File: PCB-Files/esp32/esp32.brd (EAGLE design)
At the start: 36 x 36 mm, 20 parts, among them SW1 SPST_TACT-KMR2, SW2 SPST_TACT-KMR2, X2 ESP32_WROOM32_SKINNY

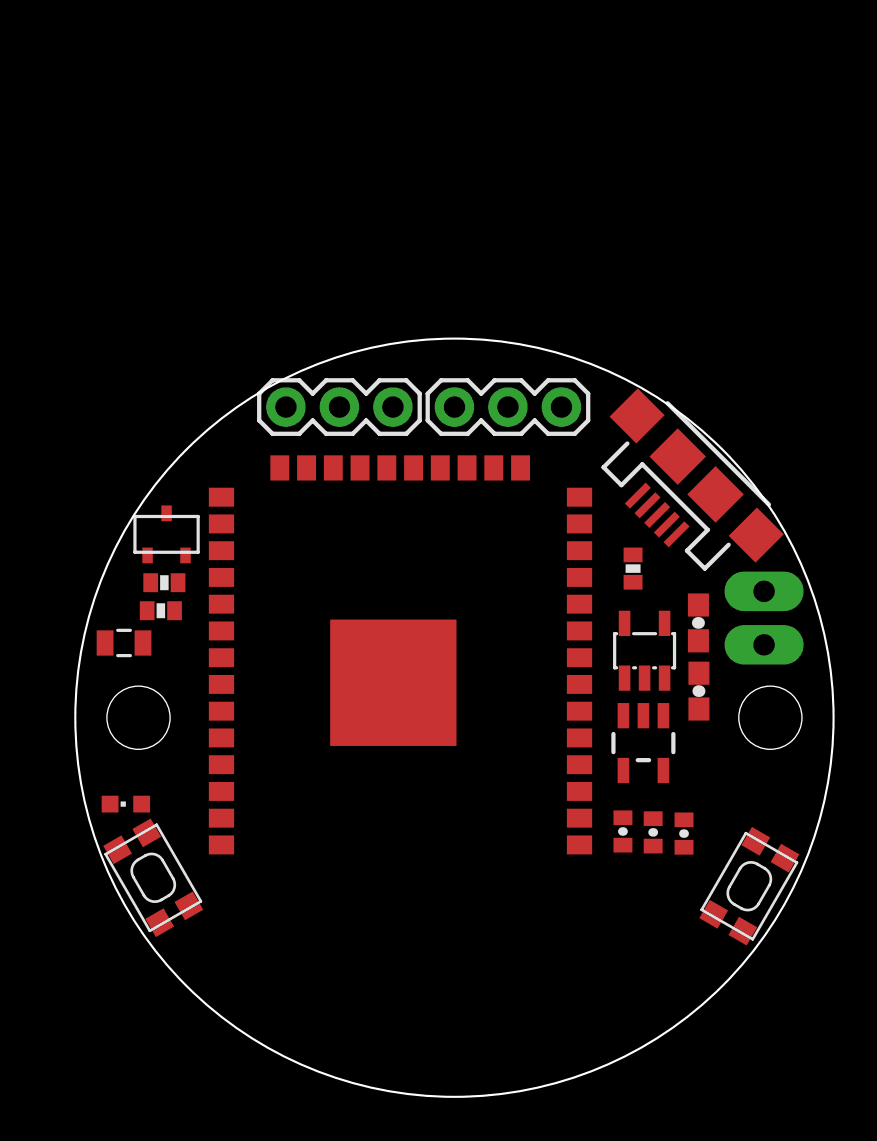
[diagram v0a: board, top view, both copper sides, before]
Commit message: rounded 4-side for class
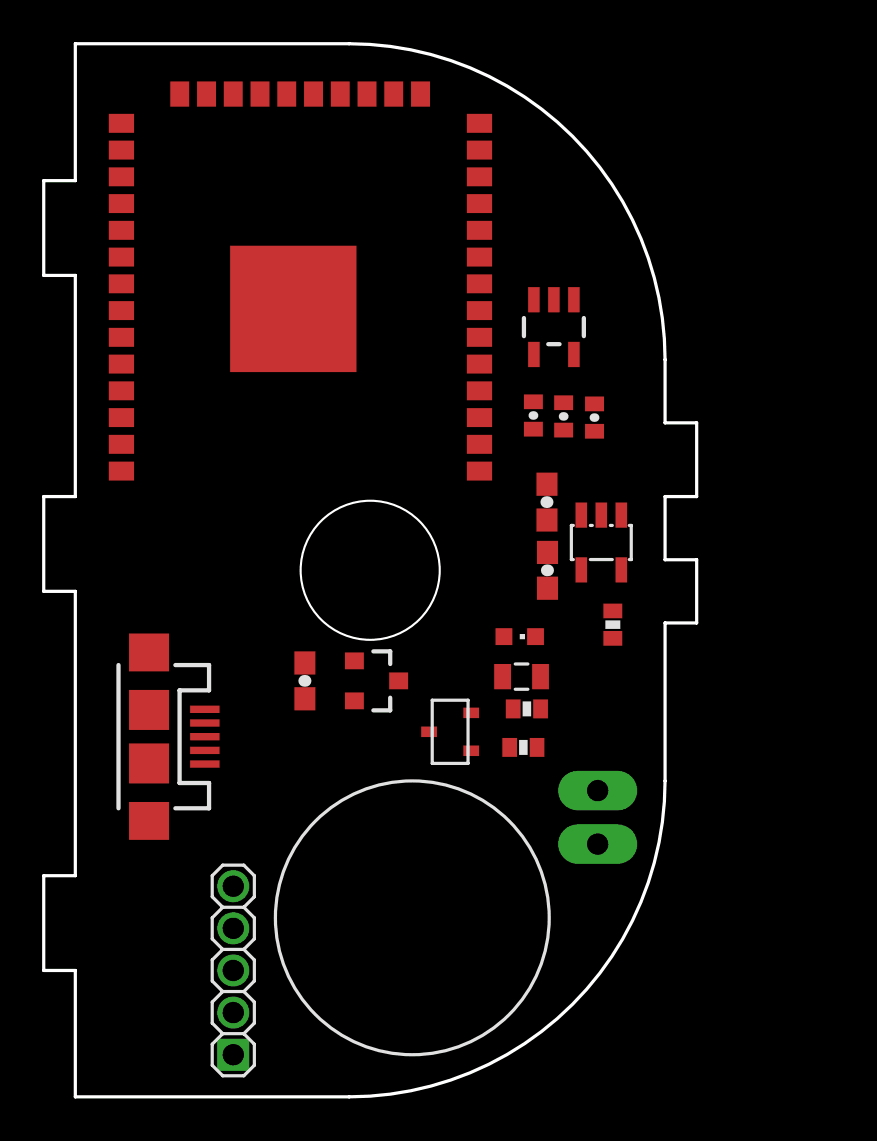
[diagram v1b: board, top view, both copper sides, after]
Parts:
- removed JP2: (no value), SparkFun:1X02_LONGPADS
- removed JP8, JP9: (no value), SparkFun:1X03
- removed SW1, SW2: SPST_TACT-KMR2, adafruit:KMR2
- added C3: 0.1uF, SparkFun:0603-CAP
- added CHARGER: MCP73831/OT, adafruit:SOT23-5L
- added HALL: HALLEFFECT-A1326, Andy_Sigler:SOT23-3
- added JP3: (no value), pinhead:1_05X2MM
- LIPO: value MCP73831/OT -> (none); device adafruit:SOT23-5L -> SparkFun:1X02_LONGPADS
- moved JP1 28.8 mm to (3.50, 17.1), turned to 270 degrees
- moved LED1 20.3 mm to (21.1, 21.9), turned to 270 degrees
- moved C2 20.2 mm to (21.8, 32.4)
- moved C4 20.2 mm to (24.6, 32.2)
- moved REG 20.2 mm to (22.7, 36.5)
- moved C10 20.2 mm to (23.2, 32.3)
- moved R6 18.9 mm to (21.2, 20.0), turned to 180 degrees
- moved R15 18.8 mm to (21.3, 16.6), turned to 0 degrees
- moved X2 18.4 mm to (10.7, 34.7)
- moved R10 18.0 mm to (21.4, 18.4), turned to 0 degrees
- moved Q1 16.4 mm to (17.8, 17.3), turned to 90 degrees
- moved C8 11.5 mm to (22.4, 28.2), turned to 90 degrees
- moved LIPO 9.45 mm to (24.8, 12.0), turned to 90 degrees
- moved C1 7.59 mm to (22.4, 25.0), turned to 90 degrees
- moved R22 2.83 mm to (25.5, 22.4), turned to 270 degrees
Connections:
- removed net HALL_1: JP8.2
- removed net HALL_2: JP9.2
- new net HALL_4: HALL.2
- net 5V: now also CHARGER.4; no longer LIPO.4
- net GND: now also CHARGER.2, JP3.1, LIPO.1; no longer JP2.1, LIPO.2, SW1.2, SW1.4, SW2.1, SW2.3
- net GPIO0: now also JP3.4; no longer SW1.1, SW1.3
- net HALL_GND: now also C3.1, HALL.3; no longer JP8.1, JP9.1
- net N$2: now also CHARGER.5; no longer LIPO.5
- net RESET: now also JP3.5; no longer SW2.2, SW2.4
- net RX: now also JP3.2; no longer JP1.D+
- net TX: now also JP3.3; no longer JP1.D-
- net VBATT: now also CHARGER.3, LIPO.2; no longer JP2.2, LIPO.3
- net VCC: now also C3.2, HALL.1; no longer JP8.3, JP9.3
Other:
- board size 36 x 36 mm -> 31 x 50 mm
